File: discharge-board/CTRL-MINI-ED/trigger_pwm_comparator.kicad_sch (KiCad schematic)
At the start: 4 parts, among them U1 LMV7219M5

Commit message: Add netlist class
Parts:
- renumbered C2 to C39, C3 to C40, R9 to R34, U1 to U8
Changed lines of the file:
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@@
 		(on_board yes)
 		(dnp no)
-		(property "Reference" "C3"
+		(property "Reference" "C40"
 			(at 73.406 100.584 0)
 			(effects
@@
 			(project "CTRL-MINI-ED"
 				(path "/3fa1ca74-4d0d-40dd-8b5c-0d4be11bd5b5/570e0384-7dea-4018-9e98-6872d1c9ffe7"
-					(reference "C3")
+					(reference "C40")
 					(unit 1)
 				)
@@
 		(on_board yes)
 		(dnp no)
-		(property "Reference" "#PWR015"
+		(property "Reference" "#PWR057"
 			(at 71.12 100.33 0)
 			(effects
@@
 			(project "CTRL-MINI-ED"
 				(path "/3fa1ca74-4d0d-40dd-8b5c-0d4be11bd5b5/570e0384-7dea-4018-9e98-6872d1c9ffe7"
-					(reference "#PWR015")
+					(reference "#PWR057")
 					(unit 1)
 				)
@@
 		(on_board yes)
 		(dnp no)
-		(property "Reference" "#PWR013"
+		(property "Reference" "#PWR054"
 			(at 81.28 62.23 0)
 			(effects
@@
 			(project "CTRL-MINI-ED"
 				(path "/3fa1ca74-4d0d-40dd-8b5c-0d4be11bd5b5/570e0384-7dea-4018-9e98-6872d1c9ffe7"
-					(reference "#PWR013")
+					(reference "#PWR054")
 					(unit 1)
 				)
@@
 		(on_board yes)
 		(dnp no)
-		(property "Reference" "U1"
+		(property "Reference" "U8"
 			(at 88.392 74.422 0)
 			(effects
@@
 			(project "CTRL-MINI-ED"
 				(path "/3fa1ca74-4d0d-40dd-8b5c-0d4be11bd5b5/570e0384-7dea-4018-9e98-6872d1c9ffe7"
-					(reference "U1")
+					(reference "U8")
 					(unit 1)
 				)
@@
 		(on_board yes)
 		(dnp no)
-		(property "Reference" "R9"
+		(property "Reference" "R34"
 			(at 73.914 44.196 90)
 			(effects
@@
 			(project "CTRL-MINI-ED"
 				(path "/3fa1ca74-4d0d-40dd-8b5c-0d4be11bd5b5/570e0384-7dea-4018-9e98-6872d1c9ffe7"
-					(reference "R9")
+					(reference "R34")
 					(unit 1)
 				)
@@
 		(on_board yes)
 		(dnp no)
-		(property "Reference" "C2"
+		(property "Reference" "C39"
 			(at 83.566 51.054 0)
 			(effects
@@
 			(project "CTRL-MINI-ED"
 				(path "/3fa1ca74-4d0d-40dd-8b5c-0d4be11bd5b5/570e0384-7dea-4018-9e98-6872d1c9ffe7"
-					(reference "C2")
+					(reference "C39")
 					(unit 1)
 				)
@@
 		(on_board yes)
 		(dnp no)
-		(property "Reference" "#PWR018"
+		(property "Reference" "#PWR058"
 			(at 71.12 114.3 0)
 			(effects
@@
 			(project "CTRL-MINI-ED"
 				(path "/3fa1ca74-4d0d-40dd-8b5c-0d4be11bd5b5/570e0384-7dea-4018-9e98-6872d1c9ffe7"
-					(reference "#PWR018")
+					(reference "#PWR058")
 					(unit 1)
 				)
@@
 		(on_board yes)
 		(dnp no)
-		(property "Reference" "#PWR014"
+		(property "Reference" "#PWR055"
 			(at 95.25 64.77 0)
 			(effects
@@
 			(project "CTRL-MINI-ED"
 				(path "/3fa1ca74-4d0d-40dd-8b5c-0d4be11bd5b5/570e0384-7dea-4018-9e98-6872d1c9ffe7"
-					(reference "#PWR014")
+					(reference "#PWR055")
 					(unit 1)
 				)
@@
 		(on_board yes)
 		(dnp no)
-		(property "Reference" "#PWR017"
+		(property "Reference" "#PWR056"
 			(at 95.25 88.9 0)
 			(effects
@@
 			(project "CTRL-MINI-ED"
 				(path "/3fa1ca74-4d0d-40dd-8b5c-0d4be11bd5b5/570e0384-7dea-4018-9e98-6872d1c9ffe7"
-					(reference "#PWR017")
-					(unit 1)
-				)
+					(reference "#PWR056")
+					(unit 1)
+				)

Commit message: Draft of PCB layout
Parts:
- added TP52: TestPoint, TestPoint:TestPoint_Pad_D1.5mm, symbol Connector:TestPoint
- renumbered R34 to R28
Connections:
- net at C39.1, R28.2, U8.4 (-): now also TP52.1
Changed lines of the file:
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@@
+		(color 0 0 0 0)
+	)
+	(junction
+		(at 101.6 48.26)
+		(diameter 0)
 		(color 0 0 0 0)
 	)
@@
 		(on_board yes)
 		(dnp no)
-		(property "Reference" "#PWR057"
+		(property "Reference" "#PWR052"
 			(at 71.12 100.33 0)
 			(effects
@@
 			(project "CTRL-MINI-ED"
 				(path "/3fa1ca74-4d0d-40dd-8b5c-0d4be11bd5b5/570e0384-7dea-4018-9e98-6872d1c9ffe7"
-					(reference "#PWR057")
+					(reference "#PWR052")
 					(unit 1)
 				)
@@
 		(on_board yes)
 		(dnp no)
-		(property "Reference" "#PWR054"
+		(property "Reference" "#PWR049"
 			(at 81.28 62.23 0)
 			(effects
@@
 			(project "CTRL-MINI-ED"
 				(path "/3fa1ca74-4d0d-40dd-8b5c-0d4be11bd5b5/570e0384-7dea-4018-9e98-6872d1c9ffe7"
-					(reference "#PWR054")
+					(reference "#PWR049")
+					(unit 1)
+				)
+			)
+		)
+	)
+	(symbol
+		(lib_id "Connector:TestPoint")
+		(at 101.6 48.26 0)
+		(unit 1)
+		(exclude_from_sim no)
+		(in_bom yes)
+		(on_board yes)
+		(dnp no)
+		(property "Reference" "TP52"
+			(at 99.822 42.926 0)
+			(effects
+				(font
+					(size 1.27 1.27)
+				)
+				(justify left)
+			)
+		)
+		(property "Value" "TestPoint"
+			(at 104.14 46.2279 0)
+			(effects
+				(font
+					(size 1.27 1.27)
+				)
+				(justify left)
+				(hide yes)
+			)
+		)
+		(property "Footprint" "TestPoint:TestPoint_Pad_D1.5mm"
+			(at 106.68 48.26 0)
+			(effects
+				(font
+					(size 1.27 1.27)
+				)
+				(hide yes)
+			)
+		)
+		(property "Datasheet" "~"
+			(at 106.68 48.26 0)
+			(effects
+				(font
+					(size 1.27 1.27)
+				)
+				(hide yes)
+			)
+		)
+		(property "Description" "test point"
+			(at 101.6 48.26 0)
+			(effects
+				(font
+					(size 1.27 1.27)
+				)
+				(hide yes)
+			)
+		)
+		(pin "1"
+		)
+		(instances
+			(project "CTRL-MINI-ED"
+				(path "/3fa1ca74-4d0d-40dd-8b5c-0d4be11bd5b5/570e0384-7dea-4018-9e98-6872d1c9ffe7"
+					(reference "TP52")
 					(unit 1)
 				)
@@
 		(on_board yes)
 		(dnp no)
-		(property "Reference" "R34"
+		(property "Reference" "R28"
 			(at 73.914 44.196 90)
 			(effects
@@
 			(project "CTRL-MINI-ED"
 				(path "/3fa1ca74-4d0d-40dd-8b5c-0d4be11bd5b5/570e0384-7dea-4018-9e98-6872d1c9ffe7"
-					(reference "R34")
+					(reference "R28")
 					(unit 1)
 				)
@@
 		(on_board yes)
 		(dnp no)
-		(property "Reference" "#PWR058"
+		(property "Reference" "#PWR053"
 			(at 71.12 114.3 0)
 			(effects
@@
 			(project "CTRL-MINI-ED"
 				(path "/3fa1ca74-4d0d-40dd-8b5c-0d4be11bd5b5/570e0384-7dea-4018-9e98-6872d1c9ffe7"
-					(reference "#PWR058")
+					(reference "#PWR053")
 					(unit 1)
 				)
@@
 		(on_board yes)
 		(dnp no)
-		(property "Reference" "#PWR055"
+		(property "Reference" "#PWR050"
 			(at 95.25 64.77 0)
 			(effects
@@
 			(project "CTRL-MINI-ED"
 				(path "/3fa1ca74-4d0d-40dd-8b5c-0d4be11bd5b5/570e0384-7dea-4018-9e98-6872d1c9ffe7"
-					(reference "#PWR055")
+					(reference "#PWR050")
 					(unit 1)
 				)
@@
 		(on_board yes)
 		(dnp no)
-		(property "Reference" "#PWR056"
+		(property "Reference" "#PWR051"
 			(at 95.25 88.9 0)
 			(effects
@@
 			(project "CTRL-MINI-ED"
 				(path "/3fa1ca74-4d0d-40dd-8b5c-0d4be11bd5b5/570e0384-7dea-4018-9e98-6872d1c9ffe7"
-					(reference "#PWR056")
+					(reference "#PWR051")
 					(unit 1)
 				)

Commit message: Cleanup old powers
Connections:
- net VDIGITAL renamed +3V3
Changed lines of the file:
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@@
+	)
+	(symbol
+		(lib_id "power:VCC")
+		(at 71.12 96.52 0)
+		(unit 1)
+		(exclude_from_sim no)
+		(in_bom yes)
+		(on_board yes)
+		(dnp no)
+		(property "Reference" "#PWR01"
+			(at 71.12 100.33 0)
+			(effects
+				(font
+					(size 1.27 1.27)
+				)
+				(hide yes)
+			)
+		)
+		(property "Value" "+3V3"
+			(at 70.866 92.202 0)
+			(effects
+				(font
+					(size 1.27 1.27)
+				)
+			)
+		)
+		(property "Footprint" ""
+			(at 71.12 96.52 0)
+			(effects
+				(font
+					(size 1.27 1.27)
+				)
+				(hide yes)
+			)
+		)
+		(property "Datasheet" ""
+			(at 71.12 96.52 0)
+			(effects
+				(font
+					(size 1.27 1.27)
+				)
+				(hide yes)
+			)
+		)
+		(property "Description" "Power symbol creates a global label with name \"VCC\""
+			(at 71.12 96.52 0)
+			(effects
+				(font
+					(size 1.27 1.27)
+				)
+				(hide yes)
+			)
+		)
+		(pin "1"
+		)
+		(instances
+			(project "CTRL-MINI-ED"
+				(path "/3fa1ca74-4d0d-40dd-8b5c-0d4be11bd5b5/570e0384-7dea-4018-9e98-6872d1c9ffe7"
+					(reference "#PWR01")
+					(unit 1)
+				)
+			)
+		)
+	)
+	(symbol
+		(lib_id "power:VCC")
+		(at 95.25 60.96 0)
+		(unit 1)
+		(exclude_from_sim no)
+		(in_bom yes)
+		(on_board yes)
+		(dnp no)
+		(property "Reference" "#PWR032"
+			(at 95.25 64.77 0)
+			(effects
+				(font
+					(size 1.27 1.27)
+				)
+				(hide yes)
+			)
+		)
+		(property "Value" "+3V3"
+			(at 94.996 56.642 0)
+			(effects
+				(font
+					(size 1.27 1.27)
+				)
+			)
+		)
+		(property "Footprint" ""
+			(at 95.25 60.96 0)
+			(effects
+				(font
+					(size 1.27 1.27)
+				)
+				(hide yes)
+			)
+		)
+		(property "Datasheet" ""
+			(at 95.25 60.96 0)
+			(effects
+				(font
+					(size 1.27 1.27)
+				)
+				(hide yes)
+			)
+		)
+		(property "Description" "Power symbol creates a global label with name \"VCC\""
+			(at 95.25 60.96 0)
+			(effects
+				(font
+					(size 1.27 1.27)
+				)
+				(hide yes)
+			)
+		)
+		(pin "1"
+		)
+		(instances
+			(project "CTRL-MINI-ED"
+				(path "/3fa1ca74-4d0d-40dd-8b5c-0d4be11bd5b5/570e0384-7dea-4018-9e98-6872d1c9ffe7"
+					(reference "#PWR032")
+					(unit 1)
+				)
+			)
+		)
 	)
 	(symbol
@@
 				(path "/3fa1ca74-4d0d-40dd-8b5c-0d4be11bd5b5/570e0384-7dea-4018-9e98-6872d1c9ffe7"
 					(reference "C40")
-					(unit 1)
-				)
-			)
-		)
-	)
-	(symbol
-		(lib_id "power:VCC")
-		(at 71.12 96.52 0)
-		(unit 1)
-		(exclude_from_sim no)
-		(in_bom yes)
-		(on_board yes)
-		(dnp no)
-		(property "Reference" "#PWR052"
-			(at 71.12 100.33 0)
-			(effects
-				(font
-					(size 1.27 1.27)
-				)
-				(hide yes)
-			)
-		)
-		(property "Value" "VDIGITAL"
-			(at 73.66 92.71 0)
-			(effects
-				(font
-					(size 1.27 1.27)
-				)
-			)
-		)
-		(property "Footprint" ""
-			(at 71.12 96.52 0)
-			(effects
-				(font
-					(size 1.27 1.27)
-				)
-				(hide yes)
-			)
-		)
-		(property "Datasheet" ""
-			(at 71.12 96.52 0)
-			(effects
-				(font
-					(size 1.27 1.27)
-				)
-				(hide yes)
-			)
-		)
-		(property "Description" "Power symbol creates a global label with name \"VCC\""
-			(at 71.12 96.52 0)
-			(effects
-				(font
-					(size 1.27 1.27)
-				)
-				(hide yes)
-			)
-		)
-		(pin "1"
-		)
-		(instances
-			(project "CTRL-MINI-ED"
-				(path "/3fa1ca74-4d0d-40dd-8b5c-0d4be11bd5b5/570e0384-7dea-4018-9e98-6872d1c9ffe7"
-					(reference "#PWR052")
 					(unit 1)
 				)
@@
 					(unit 1)
 				)
-			)
-		)
-	)
-	(symbol
-		(lib_id "power:VCC")
-		(at 95.25 60.96 0)
-		(unit 1)
-		(exclude_from_sim no)
-		(in_bom yes)
-		(on_board yes)
-		(dnp no)
-		(property "Reference" "#PWR050"
-			(at 95.25 64.77 0)
-			(effects
-				(font
-					(size 1.27 1.27)
-				)
-				(hide yes)
-			)
-		)
-		(property "Value" "VDIGITAL"
-			(at 95.25 57.15 0)
-			(effects
-				(font
-					(size 1.27 1.27)
-				)
-			)
-		)
-		(property "Footprint" ""
-			(at 95.25 60.96 0)
-			(effects
-				(font
-					(size 1.27 1.27)
-				)
-				(hide yes)
-			)
-		)
-		(property "Datasheet" ""
-			(at 95.25 60.96 0)
-			(effects
-				(font
-					(size 1.27 1.27)
-				)
-				(hide yes)
-			)
-		)
-		(property "Description" "Power symbol creates a global label with name \"VCC\""
-			(at 95.25 60.96 0)
-			(effects
-				(font
-					(size 1.27 1.27)
-				)
-				(hide yes)
-			)
-		)
-		(pin "1"
-		)
-		(instances
-			(project "CTRL-MINI-ED"
-				(path "/3fa1ca74-4d0d-40dd-8b5c-0d4be11bd5b5/570e0384-7dea-4018-9e98-6872d1c9ffe7"
-					(reference "#PWR050")
-					(unit 1)
-				)

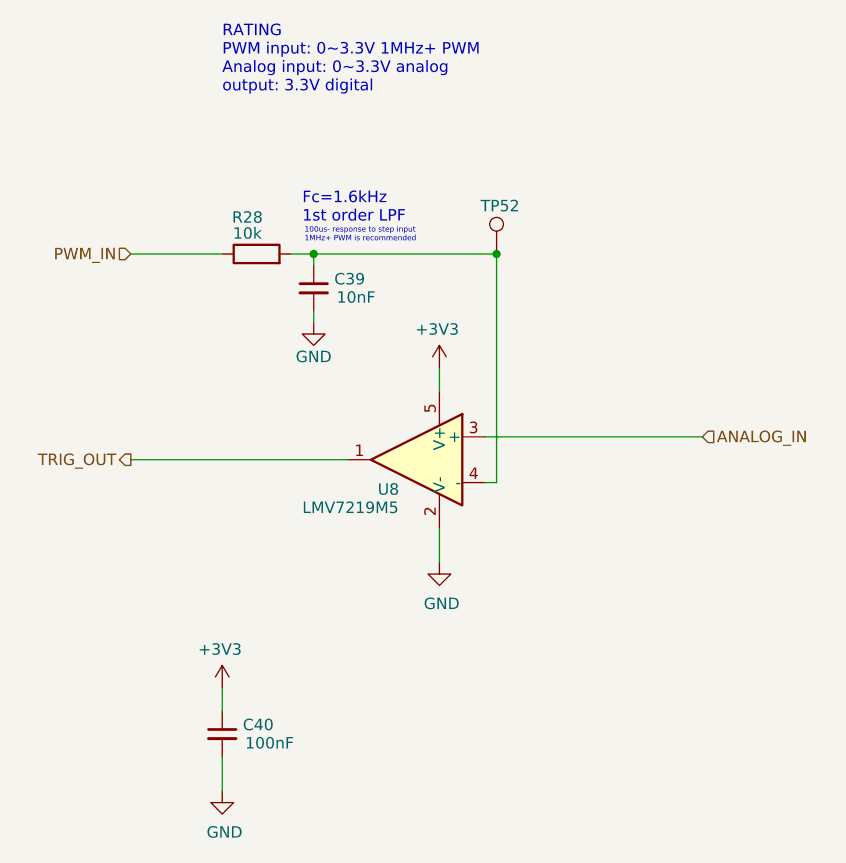
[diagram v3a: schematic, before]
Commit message: Basic building block layout
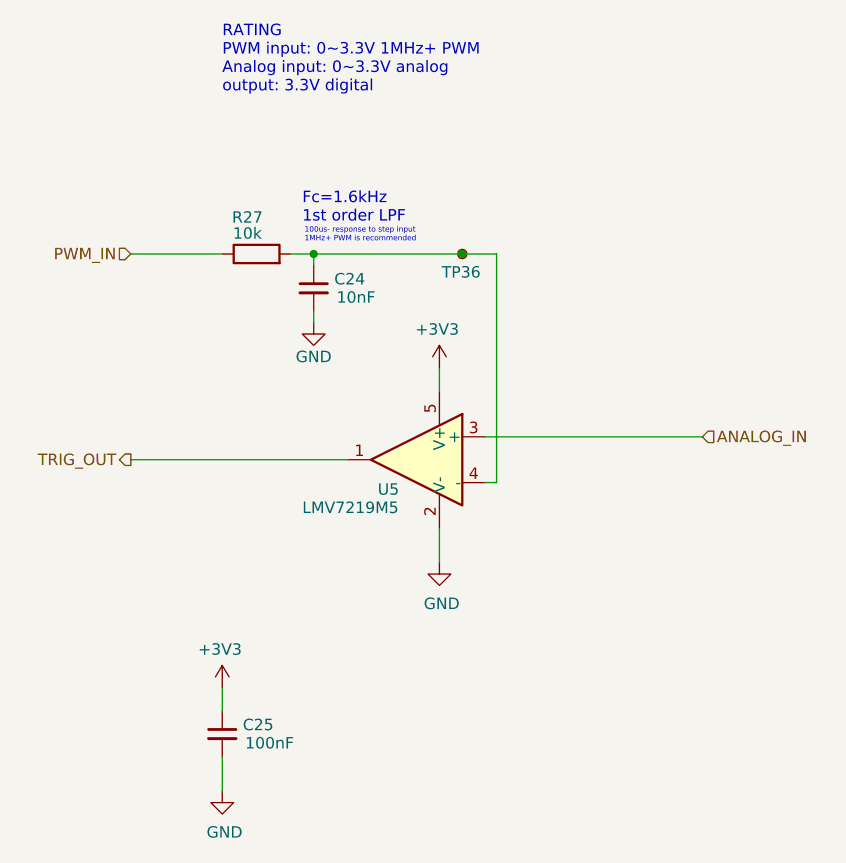
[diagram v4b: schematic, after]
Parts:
- TP36: renamed from TP52; symbol Connector:TestPoint -> Connector:TestPoint_Small
- renumbered C39 to C24, C40 to C25, R28 to R27, U8 to U5
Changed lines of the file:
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@@
 	)
 	(junction
-		(at 101.6 48.26)
+		(at 97.79 48.26)
 		(diameter 0)
 		(color 0 0 0 0)
@@
 	(wire
 		(pts
+			(xy 97.79 48.26) (xy 101.6 48.26)
+		)
+		(stroke
+			(width 0)
+			(type default)
+		)
+	)
+	(wire
+		(pts
 			(xy 95.25 60.96) (xy 95.25 63.5)
 		)
@@
 	(wire
 		(pts
-			(xy 81.28 48.26) (xy 101.6 48.26)
+			(xy 81.28 48.26) (xy 97.79 48.26)
 		)
 		(stroke
@@
 		(on_board yes)
 		(dnp no)
-		(property "Reference" "#PWR01"
+		(property "Reference" "#PWR038"
 			(at 71.12 100.33 0)
 			(effects
@@
 			(project "CTRL-MINI-ED"
 				(path "/3fa1ca74-4d0d-40dd-8b5c-0d4be11bd5b5/570e0384-7dea-4018-9e98-6872d1c9ffe7"
-					(reference "#PWR01")
+					(reference "#PWR038")
 					(unit 1)
 				)
@@
 		(on_board yes)
 		(dnp no)
-		(property "Reference" "#PWR032"
+		(property "Reference" "#PWR036"
 			(at 95.25 64.77 0)
 			(effects
@@
 			(project "CTRL-MINI-ED"
 				(path "/3fa1ca74-4d0d-40dd-8b5c-0d4be11bd5b5/570e0384-7dea-4018-9e98-6872d1c9ffe7"
-					(reference "#PWR032")
+					(reference "#PWR036")
 					(unit 1)
 				)
@@
 		(on_board yes)
 		(dnp no)
-		(property "Reference" "C40"
+		(property "Reference" "C25"
 			(at 73.406 100.584 0)
 			(effects
@@
 			(project "CTRL-MINI-ED"
 				(path "/3fa1ca74-4d0d-40dd-8b5c-0d4be11bd5b5/570e0384-7dea-4018-9e98-6872d1c9ffe7"
-					(reference "C40")
+					(reference "C25")
 					(unit 1)
 				)
@@
 		(on_board yes)
 		(dnp no)
-		(property "Reference" "#PWR049"
+		(property "Reference" "#PWR035"
 			(at 81.28 62.23 0)
 			(effects
@@
 			(project "CTRL-MINI-ED"
 				(path "/3fa1ca74-4d0d-40dd-8b5c-0d4be11bd5b5/570e0384-7dea-4018-9e98-6872d1c9ffe7"
-					(reference "#PWR049")
+					(reference "#PWR035")
 					(unit 1)
 				)
@@
 	)
 	(symbol
-		(lib_id "Connector:TestPoint")
-		(at 101.6 48.26 0)
+		(lib_id "Connector:TestPoint_Small")
+		(at 97.79 48.26 0)
 		(unit 1)
 		(exclude_from_sim no)
@@
 		(on_board yes)
 		(dnp no)
-		(property "Reference" "TP52"
-			(at 99.822 42.926 0)
+		(property "Reference" "TP36"
+			(at 95.504 50.292 0)
 			(effects
 				(font
@@
 		)
 		(property "Value" "TestPoint"
-			(at 104.14 46.2279 0)
+			(at 100.33 46.2279 0)
 			(effects
 				(font
@@
 		)
 		(property "Footprint" "TestPoint:TestPoint_Pad_D1.5mm"
-			(at 106.68 48.26 0)
+			(at 102.87 48.26 0)
 			(effects
 				(font
@@
 		)
 		(property "Datasheet" "~"
-			(at 106.68 48.26 0)
+			(at 102.87 48.26 0)
 			(effects
 				(font
@@
 		)
 		(property "Description" "test point"
-			(at 101.6 48.26 0)
+			(at 97.79 48.26 0)
 			(effects
 				(font
@@
 			(project "CTRL-MINI-ED"
 				(path "/3fa1ca74-4d0d-40dd-8b5c-0d4be11bd5b5/570e0384-7dea-4018-9e98-6872d1c9ffe7"
-					(reference "TP52")
+					(reference "TP36")
 					(unit 1)
 				)
@@
 		(on_board yes)
 		(dnp no)
-		(property "Reference" "U8"
+		(property "Reference" "U5"
 			(at 88.392 74.422 0)
 			(effects
@@
 			(project "CTRL-MINI-ED"
 				(path "/3fa1ca74-4d0d-40dd-8b5c-0d4be11bd5b5/570e0384-7dea-4018-9e98-6872d1c9ffe7"
-					(reference "U8")
+					(reference "U5")
 					(unit 1)
 				)
@@
 		(on_board yes)
 		(dnp no)
-		(property "Reference" "R28"
+		(property "Reference" "R27"
 			(at 73.914 44.196 90)
 			(effects
@@
 			(project "CTRL-MINI-ED"
 				(path "/3fa1ca74-4d0d-40dd-8b5c-0d4be11bd5b5/570e0384-7dea-4018-9e98-6872d1c9ffe7"
-					(reference "R28")
+					(reference "R27")
 					(unit 1)
 				)
@@
 		(on_board yes)
 		(dnp no)
-		(property "Reference" "C39"
+		(property "Reference" "C24"
 			(at 83.566 51.054 0)
 			(effects
@@
 			(project "CTRL-MINI-ED"
 				(path "/3fa1ca74-4d0d-40dd-8b5c-0d4be11bd5b5/570e0384-7dea-4018-9e98-6872d1c9ffe7"
-					(reference "C39")
+					(reference "C24")
 					(unit 1)
 				)
@@
 		(on_board yes)
 		(dnp no)
-		(property "Reference" "#PWR053"
+		(property "Reference" "#PWR039"
 			(at 71.12 114.3 0)
 			(effects
@@
 			(project "CTRL-MINI-ED"
 				(path "/3fa1ca74-4d0d-40dd-8b5c-0d4be11bd5b5/570e0384-7dea-4018-9e98-6872d1c9ffe7"
-					(reference "#PWR053")
+					(reference "#PWR039")
 					(unit 1)
 				)
@@
 		(on_board yes)
 		(dnp no)
-		(property "Reference" "#PWR051"
+		(property "Reference" "#PWR037"
 			(at 95.25 88.9 0)
 			(effects
@@
 			(project "CTRL-MINI-ED"
 				(path "/3fa1ca74-4d0d-40dd-8b5c-0d4be11bd5b5/570e0384-7dea-4018-9e98-6872d1c9ffe7"
-					(reference "#PWR051")
+					(reference "#PWR037")
 					(unit 1)
 				)
